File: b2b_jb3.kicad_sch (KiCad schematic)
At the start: 11 parts

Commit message: edit README.md
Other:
- company: (none) -> NOIRLab
- title: (none) -> 4 channel ADC Module
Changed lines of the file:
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@@
 	(generator_version "9.0")
 	(paper "A4")
+	(title_block
+		(title "4 channel ADC Module")
+		(date "2025-04-18")
+		(rev "0.1")
+		(company "NOIRLab")
+		(comment 1 "Design: Braulio Cancino Vera - braulio.cancino@noirlab.edu")
+	)
 	(text "MRCC: Multi-Region Clock Capable"
 		(exclude_from_sim no)

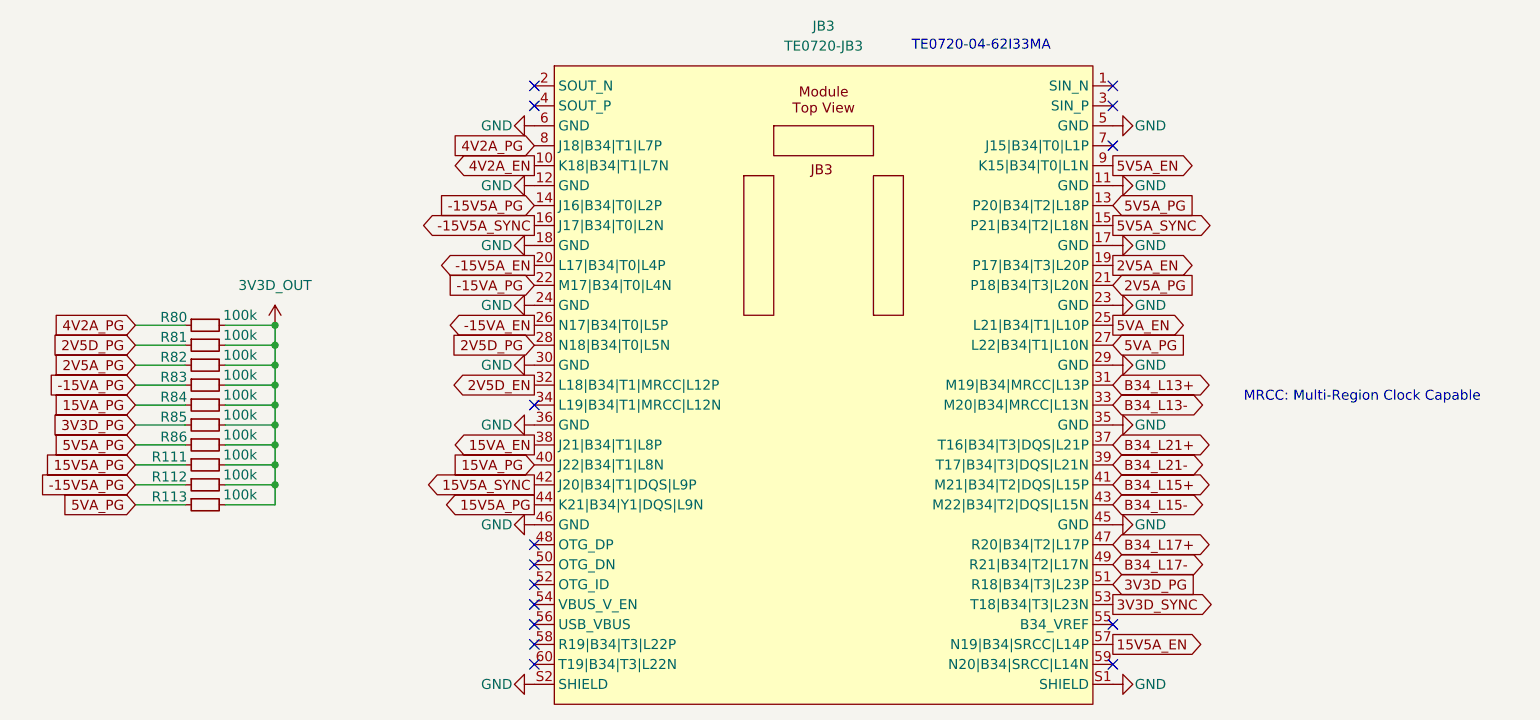
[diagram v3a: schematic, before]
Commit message: Split DC DC schematic and improve layout
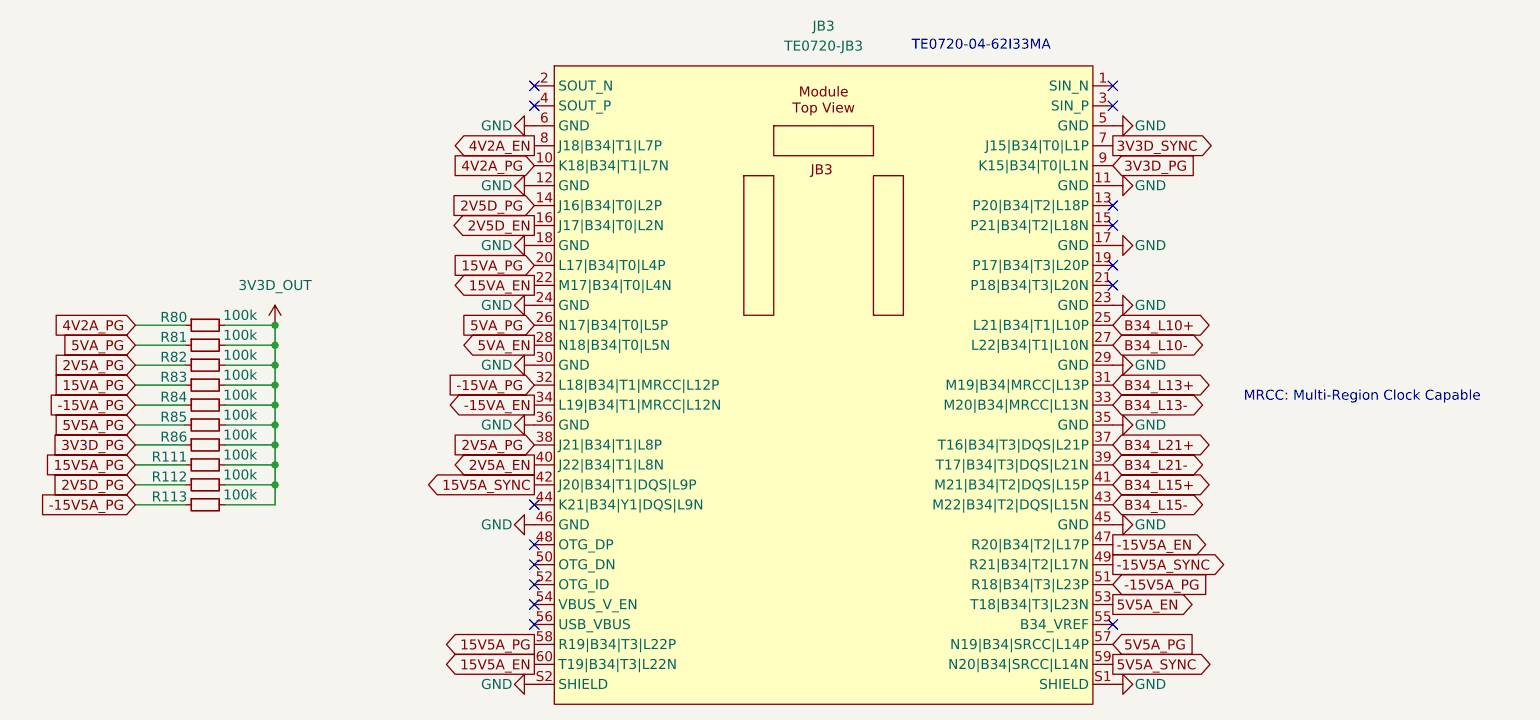
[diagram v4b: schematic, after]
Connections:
- net B34_L17+ is gone; now on net -15V5A_EN: JB3.47 (R20|B34|T2|L17P)
- net B34_L17- is gone; now on net -15V5A_SYNC: JB3.49 (R21|B34|T2|L17N)
- net -15V5A_EN: no longer JB3.20 (L17|B34|T0|L4P)
- net -15V5A_PG: now also JB3.51 (R18|B34|T3|L23P), R113.1; no longer JB3.14 (J16|B34|T0|L2P), R112.1
- net -15V5A_SYNC: no longer JB3.16 (J17|B34|T0|L2N)
- net -15VA_EN: now also JB3.34 (L19|B34|T1|MRCC|L12N); no longer JB3.26 (N17|B34|T0|L5P)
- net -15VA_PG: now also JB3.32 (L18|B34|T1|MRCC|L12P), R84.1; no longer JB3.22 (M17|B34|T0|L4N), R83.1
- net 15V5A_EN: now also JB3.60 (T19|B34|T3|L22N); no longer JB3.57 (N19|B34|SRCC|L14P)
- net 15V5A_PG: now also JB3.58 (R19|B34|T3|L22P); no longer JB3.44 (K21|B34|Y1|DQS|L9N)
- net 15VA_EN: now also JB3.22 (M17|B34|T0|L4N); no longer JB3.38 (J21|B34|T1|L8P)
- net 15VA_PG: now also JB3.20 (L17|B34|T0|L4P), R83.1; no longer JB3.40 (J22|B34|T1|L8N), R84.1
- net 2V5A_EN: now also JB3.40 (J22|B34|T1|L8N); no longer JB3.19 (P17|B34|T3|L20P)
- net 2V5A_PG: now also JB3.38 (J21|B34|T1|L8P); no longer JB3.21 (P18|B34|T3|L20N)
- net 2V5D_EN: now also JB3.16 (J17|B34|T0|L2N); no longer JB3.32 (L18|B34|T1|MRCC|L12P)
- net 2V5D_PG: now also JB3.14 (J16|B34|T0|L2P), R112.1; no longer JB3.28 (N18|B34|T0|L5N), R81.1
- net 3V3D_PG: now also JB3.9 (K15|B34|T0|L1N), R86.1; no longer JB3.51 (R18|B34|T3|L23P), R85.1
- net 3V3D_SYNC: now also JB3.7 (J15|B34|T0|L1P); no longer JB3.53 (T18|B34|T3|L23N)
- net 4V2A_EN: now also JB3.8 (J18|B34|T1|L7P); no longer JB3.10 (K18|B34|T1|L7N)
- net 4V2A_PG: now also JB3.10 (K18|B34|T1|L7N); no longer JB3.8 (J18|B34|T1|L7P)
- net 5V5A_EN: now also JB3.53 (T18|B34|T3|L23N); no longer JB3.9 (K15|B34|T0|L1N)
- net 5V5A_PG: now also JB3.57 (N19|B34|SRCC|L14P), R85.1; no longer JB3.13 (P20|B34|T2|L18P), R86.1
- net 5V5A_SYNC: now also JB3.59 (N20|B34|SRCC|L14N); no longer JB3.15 (P21|B34|T2|L18N)
- net 5VA_EN: now also JB3.28 (N18|B34|T0|L5N); no longer JB3.25 (L21|B34|T1|L10P)
- net 5VA_PG: now also JB3.26 (N17|B34|T0|L5P), R81.1; no longer JB3.27 (L22|B34|T1|L10N), R113.1
- new net B34_L10+: JB3.25 (L21|B34|T1|L10P)
- new net B34_L10-: JB3.27 (L22|B34|T1|L10N)

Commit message: Improve layout
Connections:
- net -15VA_EN: now also JB3.28 (N18|B34|T0|L5N); no longer JB3.34 (L19|B34|T1|MRCC|L12N)
- net -15VA_PG: now also JB3.26 (N17|B34|T0|L5P), R81.1; no longer JB3.32 (L18|B34|T1|MRCC|L12P), R84.1
- net 15VA_EN: now also JB3.16 (J17|B34|T0|L2N); no longer JB3.22 (M17|B34|T0|L4N)
- net 15VA_PG: now also JB3.14 (J16|B34|T0|L2P), R112.1; no longer JB3.20 (L17|B34|T0|L4P), R83.1
- net 2V5A_EN: now also JB3.34 (L19|B34|T1|MRCC|L12N); no longer JB3.40 (J22|B34|T1|L8N)
- net 2V5A_PG: now also JB3.32 (L18|B34|T1|MRCC|L12P), R84.1; no longer JB3.38 (J21|B34|T1|L8P), R82.1
- net 2V5D_EN: now also JB3.10 (K18|B34|T1|L7N); no longer JB3.16 (J17|B34|T0|L2N)
- net 2V5D_PG: now also JB3.8 (J18|B34|T1|L7P), R80.1; no longer JB3.14 (J16|B34|T0|L2P), R112.1
- net 4V2A_EN: now also JB3.40 (J22|B34|T1|L8N); no longer JB3.8 (J18|B34|T1|L7P)
- net 4V2A_PG: now also JB3.38 (J21|B34|T1|L8P), R82.1; no longer JB3.10 (K18|B34|T1|L7N), R80.1
- net 5VA_EN: now also JB3.22 (M17|B34|T0|L4N); no longer JB3.28 (N18|B34|T0|L5N)
- net 5VA_PG: now also JB3.20 (L17|B34|T0|L4P), R83.1; no longer JB3.26 (N17|B34|T0|L5P), R81.1
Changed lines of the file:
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@@
 	(title_block
 		(title "4 channel ADC Module")
-		(date "2025-05-21")
+		(date "2025-06-03")
 		(rev "0.1")
 		(company "NOIRLab")
@@
 	(global_label "-15VA_PG"
 		(shape input)
-		(at 83.82 96.52 180)
-		(fields_autoplaced yes)
-		(effects
-			(font
-				(size 1.27 1.27)
-			)
-			(justify right)
-		)
-		(property "Intersheetrefs" "${INTERSHEET_REFS}"
-			(at 72.731 96.52 0)
+		(at 83.82 88.9 180)
+		(fields_autoplaced yes)
+		(effects
+			(font
+				(size 1.27 1.27)
+			)
+			(justify right)
+		)
+		(property "Intersheetrefs" "${INTERSHEET_REFS}"
+			(at 72.5496 88.9 0)
 			(effects
 				(font
@@
 	(global_label "5VA_EN"
 		(shape output)
-		(at 134.62 88.9 180)
-		(fields_autoplaced yes)
-		(effects
-			(font
-				(size 1.27 1.27)
-			)
-			(justify right)
-		)
-		(property "Intersheetrefs" "${INTERSHEET_REFS}"
-			(at 123.3496 88.9 0)
+		(at 134.62 81.28 180)
+		(fields_autoplaced yes)
+		(effects
+			(font
+				(size 1.27 1.27)
+			)
+			(justify right)
+		)
+		(property "Intersheetrefs" "${INTERSHEET_REFS}"
+			(at 121.9586 81.28 0)
 			(effects
 				(font
@@
 	(global_label "2V5A_EN"
 		(shape output)
-		(at 134.62 104.14 180)
-		(fields_autoplaced yes)
-		(effects
-			(font
-				(size 1.27 1.27)
-			)
-			(justify right)
-		)
-		(property "Intersheetrefs" "${INTERSHEET_REFS}"
-			(at 123.5915 104.14 0)
+		(at 134.62 96.52 180)
+		(fields_autoplaced yes)
+		(effects
+			(font
+				(size 1.27 1.27)
+			)
+			(justify right)
+		)
+		(property "Intersheetrefs" "${INTERSHEET_REFS}"
+			(at 122.0191 96.52 0)
 			(effects
 				(font
@@
 	(global_label "2V5D_PG"
 		(shape input)
-		(at 83.82 106.68 180)
-		(fields_autoplaced yes)
-		(effects
-			(font
-				(size 1.27 1.27)
-			)
-			(justify right)
-		)
-		(property "Intersheetrefs" "${INTERSHEET_REFS}"
-			(at 69.9491 106.68 0)
+		(at 83.82 86.36 180)
+		(fields_autoplaced yes)
+		(effects
+			(font
+				(size 1.27 1.27)
+			)
+			(justify right)
+		)
+		(property "Intersheetrefs" "${INTERSHEET_REFS}"
+			(at 72.731 86.36 0)
 			(effects
 				(font
@@
 	(global_label "5VA_PG"
 		(shape input)
-		(at 83.82 88.9 180)
-		(fields_autoplaced yes)
-		(effects
-			(font
-				(size 1.27 1.27)
-			)
-			(justify right)
-		)
-		(property "Intersheetrefs" "${INTERSHEET_REFS}"
-			(at 72.5496 88.9 0)
+		(at 83.82 93.98 180)
+		(fields_autoplaced yes)
+		(effects
+			(font
+				(size 1.27 1.27)
+			)
+			(justify right)
+		)
+		(property "Intersheetrefs" "${INTERSHEET_REFS}"
+			(at 71.1586 93.98 0)
 			(effects
 				(font
@@
 	(global_label "5VA_PG"
 		(shape input)
-		(at 134.62 86.36 180)
-		(fields_autoplaced yes)
-		(effects
-			(font
-				(size 1.27 1.27)
-			)
-			(justify right)
-		)
-		(property "Intersheetrefs" "${INTERSHEET_REFS}"
-			(at 121.1724 86.36 0)
+		(at 134.62 78.74 180)
+		(fields_autoplaced yes)
+		(effects
+			(font
+				(size 1.27 1.27)
+			)
+			(justify right)
+		)
+		(property "Intersheetrefs" "${INTERSHEET_REFS}"
+			(at 120.8096 78.74 0)
 			(effects
 				(font
@@
 	(global_label "2V5A_PG"
 		(shape input)
-		(at 134.62 101.6 180)
-		(fields_autoplaced yes)
-		(effects
-			(font
-				(size 1.27 1.27)
-			)
-			(justify right)
-		)
-		(property "Intersheetrefs" "${INTERSHEET_REFS}"
-			(at 123.531 101.6 0)
+		(at 134.62 93.98 180)
+		(fields_autoplaced yes)
+		(effects
+			(font
+				(size 1.27 1.27)
+			)
+			(justify right)
+		)
+		(property "Intersheetrefs" "${INTERSHEET_REFS}"
+			(at 119.6 93.98 0)
 			(effects
 				(font
@@
 	(global_label "-15VA_EN"
 		(shape output)
-		(at 134.62 96.52 180)
-		(fields_autoplaced yes)
-		(effects
-			(font
-				(size 1.27 1.27)
-			)
-			(justify right)
-		)
-		(property "Intersheetrefs" "${INTERSHEET_REFS}"
-			(at 122.0191 96.52 0)
+		(at 134.62 88.9 180)
+		(fields_autoplaced yes)
+		(effects
+			(font
+				(size 1.27 1.27)
+			)
+			(justify right)
+		)
+		(property "Intersheetrefs" "${INTERSHEET_REFS}"
+			(at 123.3496 88.9 0)
 			(effects
 				(font
@@
 	(global_label "4V2A_EN"
 		(shape output)
-		(at 134.62 63.5 180)
-		(fields_autoplaced yes)
-		(effects
-			(font
-				(size 1.27 1.27)
-			)
-			(justify right)
-		)
-		(property "Intersheetrefs" "${INTERSHEET_REFS}"
-			(at 123.3496 63.5 0)
+		(at 134.62 104.14 180)
+		(fields_autoplaced yes)
+		(effects
+			(font
+				(size 1.27 1.27)
+			)
+			(justify right)
+		)
+		(property "Intersheetrefs" "${INTERSHEET_REFS}"
+			(at 123.5915 104.14 0)
 			(effects
 				(font
@@
 	(global_label "4V2A_PG"
 		(shape input)
-		(at 134.62 66.04 180)
-		(fields_autoplaced yes)
-		(effects
-			(font
-				(size 1.27 1.27)
-			)
-			(justify right)
-		)
-		(property "Intersheetrefs" "${INTERSHEET_REFS}"
-			(at 123.531 66.04 0)
+		(at 134.62 101.6 180)
+		(fields_autoplaced yes)
+		(effects
+			(font
+				(size 1.27 1.27)
+			)
+			(justify right)
+		)
+		(property "Intersheetrefs" "${INTERSHEET_REFS}"
+			(at 123.531 101.6 0)
 			(effects
 				(font
@@
 	(global_label "-15VA_PG"
 		(shape input)
-		(at 134.62 93.98 180)
-		(fields_autoplaced yes)
-		(effects
-			(font
-				(size 1.27 1.27)
-			)
-			(justify right)
-		)
-		(property "Intersheetrefs" "${INTERSHEET_REFS}"
-			(at 119.6 93.98 0)
+		(at 134.62 86.36 180)
+		(fields_autoplaced yes)
+		(effects
+			(font
+				(size 1.27 1.27)
+			)
+			(justify right)
+		)
+		(property "Intersheetrefs" "${INTERSHEET_REFS}"
+			(at 121.1724 86.36 0)
 			(effects
 				(font
@@
 	(global_label "15VA_PG"
 		(shape input)
-		(at 134.62 78.74 180)
-		(fields_autoplaced yes)
-		(effects
-			(font
-				(size 1.27 1.27)
-			)
-			(justify right)
-		)
-		(property "Intersheetrefs" "${INTERSHEET_REFS}"
-			(at 120.8096 78.74 0)
+		(at 134.62 71.12 180)
+		(fields_autoplaced yes)
+		(effects
+			(font
+				(size 1.27 1.27)
+			)
+			(justify right)
+		)
+		(property "Intersheetrefs" "${INTERSHEET_REFS}"
+			(at 121.9586 71.12 0)
 			(effects
 				(font
@@
 	(global_label "4V2A_PG"
 		(shape input)
-		(at 83.82 86.36 180)
-		(fields_autoplaced yes)
-		(effects
-			(font
-				(size 1.27 1.27)
-			)
-			(justify right)
-		)
-		(property "Intersheetrefs" "${INTERSHEET_REFS}"
-			(at 72.731 86.36 0)
+		(at 83.82 91.44 180)
+		(fields_autoplaced yes)
+		(effects
+			(font
+				(size 1.27 1.27)
+			)
+			(justify right)
+		)
+		(property "Intersheetrefs" "${INTERSHEET_REFS}"
+			(at 72.731 91.44 0)
 			(effects
 				(font
@@
 	(global_label "2V5A_PG"
 		(shape input)
-		(at 83.82 91.44 180)
-		(fields_autoplaced yes)
-		(effects
-			(font
-				(size 1.27 1.27)
-			)
-			(justify right)
-		)
-		(property "Intersheetrefs" "${INTERSHEET_REFS}"
-			(at 72.731 91.44 0)
+		(at 83.82 96.52 180)
+		(fields_autoplaced yes)
+		(effects
+			(font
+				(size 1.27 1.27)
+			)
+			(justify right)
+		)
+		(property "Intersheetrefs" "${INTERSHEET_REFS}"
+			(at 72.731 96.52 0)
 			(effects
 				(font
@@
 	(global_label "2V5D_EN"
 		(shape output)
-		(at 134.62 73.66 180)
-		(fields_autoplaced yes)
-		(effects
-			(font
-				(size 1.27 1.27)
-			)
-			(justify right)
-		)
-		(property "Intersheetrefs" "${INTERSHEET_REFS}"
-			(at 118.3905 73.66 0)
+		(at 134.62 66.04 180)
+		(fields_autoplaced yes)
+		(effects
+			(font
+				(size 1.27 1.27)
+			)
+			(justify right)
+		)
+		(property "Intersheetrefs" "${INTERSHEET_REFS}"
+			(at 123.531 66.04 0)
 			(effects
 				(font
@@
 	(global_label "2V5D_PG"
 		(shape input)
-		(at 134.62 71.12 180)
-		(fields_autoplaced yes)
-		(effects
-			(font
-				(size 1.27 1.27)
-			)
-			(justify right)
-		)
-		(property "Intersheetrefs" "${INTERSHEET_REFS}"
-			(at 121.9586 71.12 0)
+		(at 134.62 63.5 180)
+		(fields_autoplaced yes)
+		(effects
+			(font
+				(size 1.27 1.27)
+			)
+			(justify right)
+		)
+		(property "Intersheetrefs" "${INTERSHEET_REFS}"
+			(at 123.3496 63.5 0)
 			(effects
 				(font
@@
 	(global_label "15VA_PG"
 		(shape input)
-		(at 83.82 93.98 180)
-		(fields_autoplaced yes)
-		(effects
-			(font
-				(size 1.27 1.27)
-			)
-			(justify right)
-		)
-		(property "Intersheetrefs" "${INTERSHEET_REFS}"
-			(at 71.1586 93.98 0)
+		(at 83.82 106.68 180)
+		(fields_autoplaced yes)
+		(effects
+			(font
+				(size 1.27 1.27)
+			)
+			(justify right)
+		)
+		(property "Intersheetrefs" "${INTERSHEET_REFS}"
+			(at 69.9491 106.68 0)
 			(effects
 				(font
@@
 	(global_label "15VA_EN"
 		(shape output)
-		(at 134.62 81.28 180)
-		(fields_autoplaced yes)
-		(effects
-			(font
-				(size 1.27 1.27)
-			)
-			(justify right)
-		)
-		(property "Intersheetrefs" "${INTERSHEET_REFS}"
-			(at 121.9586 81.28 0)
-			(effects
-				(font
+		(at 134.62 73.66 180)
+		(fields_autoplaced yes)
+		(effects
+			(font
+				(size 1.27 1.27)
+			)
+			(justify right)
+		)
+		(property "Intersheetrefs" "${INTERSHEET_REFS}"
+			(at 118.3905 73.66 0)
+			(effects
+				(font
